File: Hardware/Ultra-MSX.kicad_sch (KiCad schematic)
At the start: 11 parts, among them J7 AM4_bracket, J8 AM4_bracket

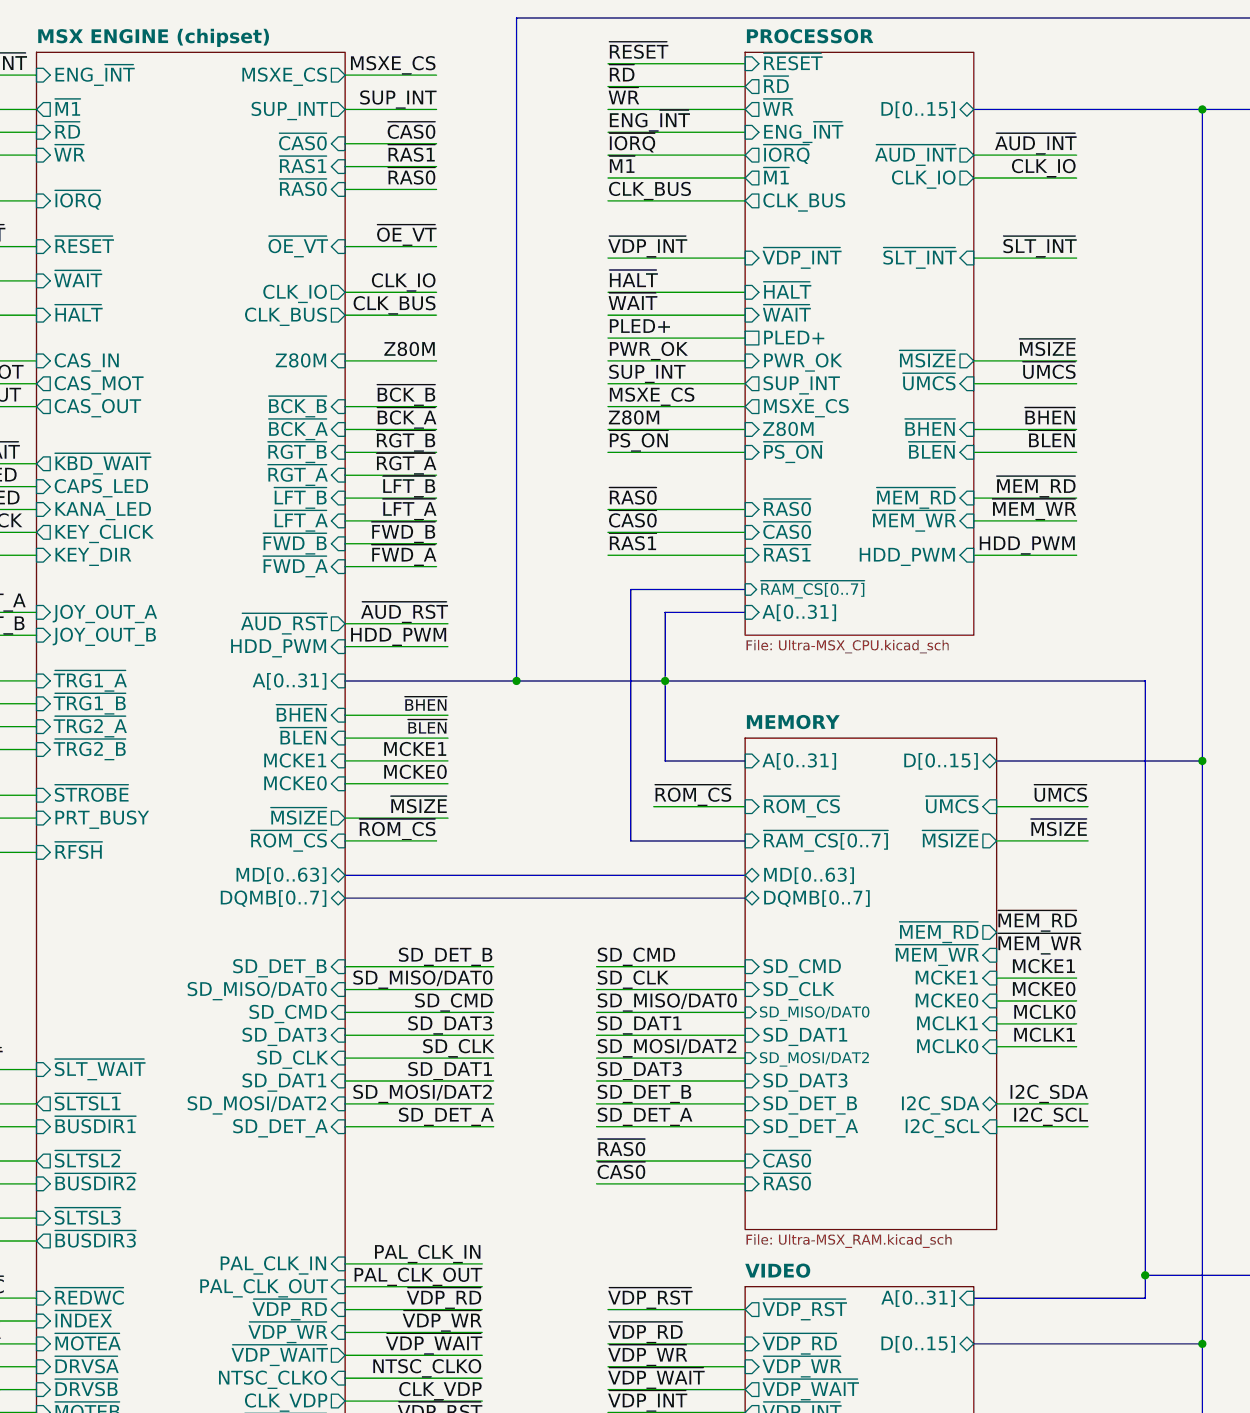
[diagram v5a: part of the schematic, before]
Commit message: Returned to Simm-72 memory module to simplify design, returned to AT40K40 with 254 io, FPGA.
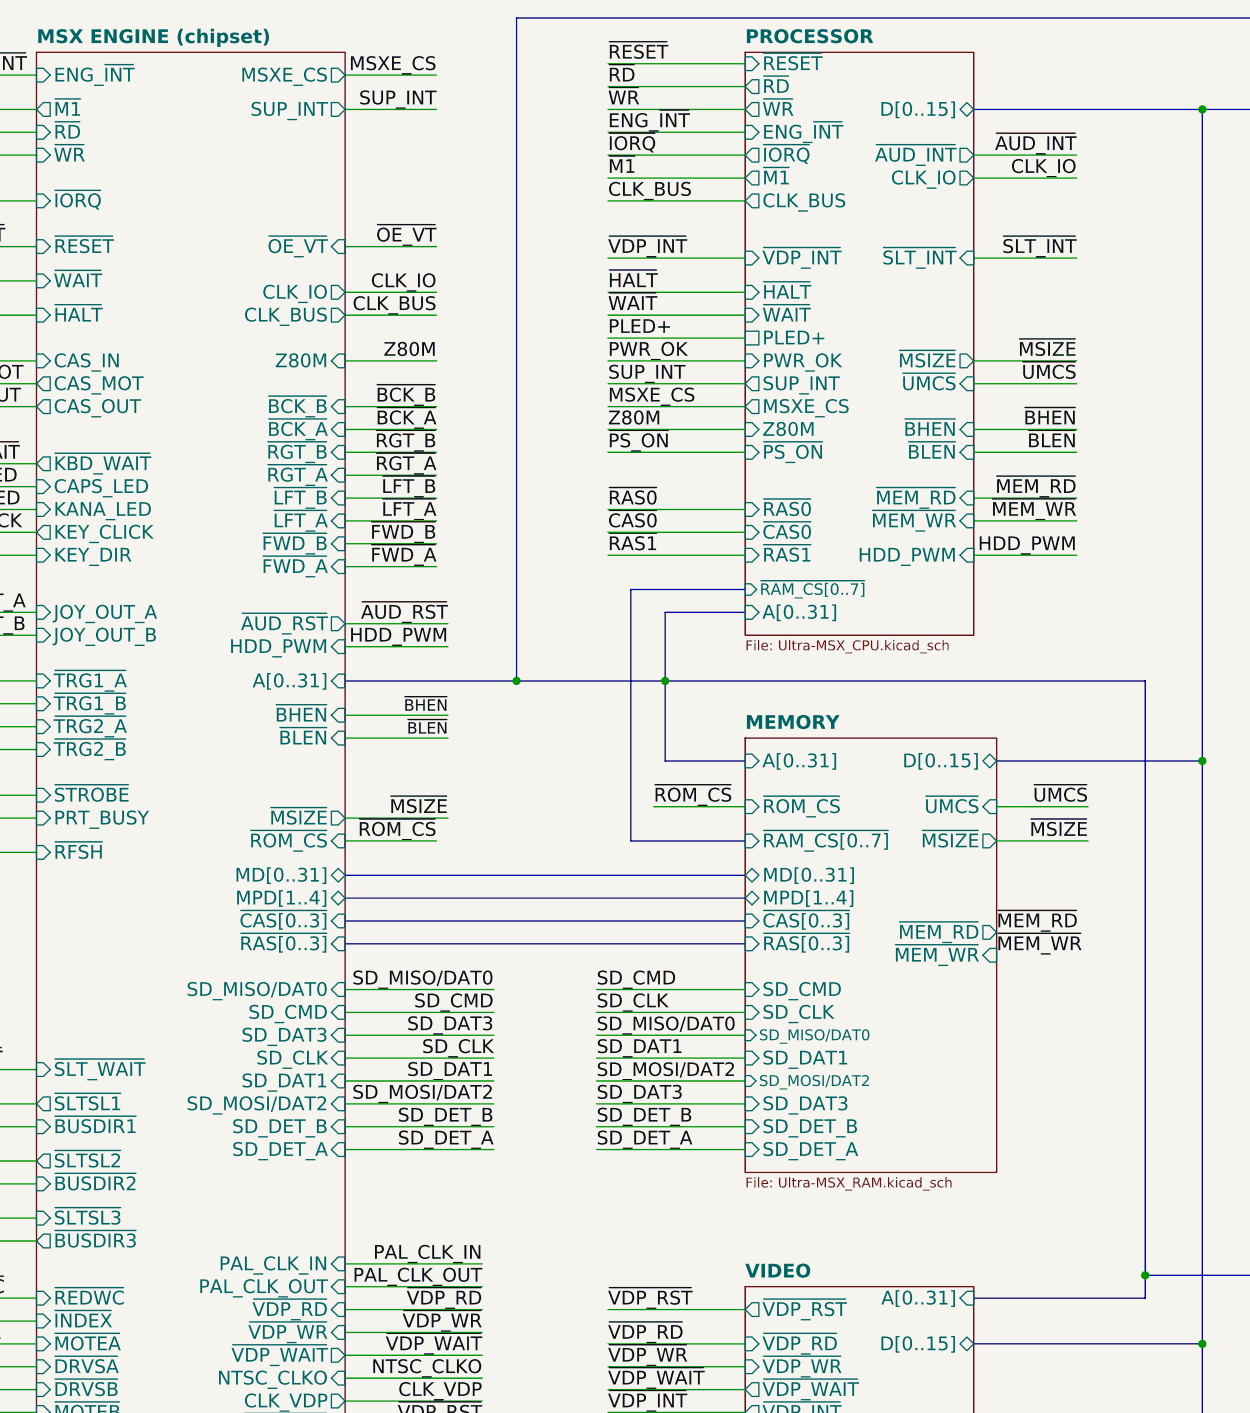
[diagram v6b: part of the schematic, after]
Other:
- sheet MEMORY ports: added MD[0..31], MPD[1..4], ~{CAS[0..3]}, ~{RAS[0..3]}; removed DQMB[0..7], I2C_SCL, I2C_SDA, MCKE0, MCKE1, MCLK0, MCLK1, MD[0..63], ~{CAS0}, ~{RAS0}
- sheet MSX ENGINE (chipset) ports: added MD[0..31], MPD[1..4], ~{CAS[0..3]}, ~{RAS[0..3]}; removed DQMB[0..7], MCKE0, MCKE1, MD[0..63], ~{CAS0}, ~{RAS0}, ~{RAS1}
